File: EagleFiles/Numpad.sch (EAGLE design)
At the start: 67 parts, among them X1 52559-2492

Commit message: Readme added
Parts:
- removed COMM: SJ-43514_HEADPHONES_3.5MM_X4, my_parts:SJ-43514_HEADPHONES_3.5MM_X4
- removed R4, R5: 3.3K, resistor:R-US_0207/10
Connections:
- removed net N$51: COMM.4, R4.2, R5.1
- removed net N$52: COMM.3, R5.2
- removed net N$53: COMM.2, R4.1
- net GND: no longer COMM.1
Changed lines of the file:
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@@
 </classes>
 <parts>
-<part name="COMM" library="my_parts" deviceset="SJ-43514_HEADPHONES_3.5MM_X4" device=""/>
-<part name="SUPPLY3" library="supply2" deviceset="GND" device=""/>
-<part name="R4" library="resistor" deviceset="R-US_" device="0207/10" value="3.3K"/>
-<part name="R5" library="resistor" deviceset="R-US_" device="0207/10" value="3.3K"/>
 <part name="U$35" library="STM32F10x F4xx" deviceset="STM32F405/415_LQFP64" device=""/>
 <part name="C1" library="resistor" library_urn="urn:adsk.eagle:library:348" deviceset="C-US" device="C0603" package3d_urn="urn:adsk.eagle:package:23616/2" value="4.7uF"/>
@@
 </plain>
 <instances>
-<instance part="COMM" gate="G$1" x="-93.98" y="110.49" smashed="yes"/>
-<instance part="SUPPLY3" gate="GND" x="-80.01" y="97.79" smashed="yes">
-<attribute name="VALUE" x="-81.915" y="94.615" size="1.778" layer="96"/>
-</instance>
-<instance part="R4" gate="G$1" x="-54.61" y="123.19" smashed="yes" rot="R90">
-<attribute name="NAME" x="-56.1086" y="119.38" size="1.778" layer="95" rot="R90"/>
-<attribute name="VALUE" x="-51.308" y="119.38" size="1.778" layer="96" rot="R90"/>
-</instance>
-<instance part="R5" gate="G$1" x="-54.61" y="102.87" smashed="yes" rot="R90">
-<attribute name="NAME" x="-56.1086" y="99.06" size="1.778" layer="95" rot="R90"/>
-<attribute name="VALUE" x="-51.308" y="99.06" size="1.778" layer="96" rot="R90"/>
-</instance>
 <instance part="U$35" gate="G$1" x="86.24" y="83.92" smashed="yes" rot="R90"/>
 <instance part="C1" gate="G$1" x="119.26" y="35.66" smashed="yes">
@@
 <nets>
 <net name="GND" class="0">
-<segment>
-<pinref part="SUPPLY3" gate="GND" pin="GND"/>
-<pinref part="COMM" gate="G$1" pin="1"/>
-<wire x1="-80.01" y1="100.33" x2="-80.01" y2="102.87" width="0.1524" layer="91"/>
-<wire x1="-80.01" y1="102.87" x2="-81.28" y2="102.87" width="0.1524" layer="91"/>
-</segment>
 <segment>
 <pinref part="C_VCAP2" gate="G$1" pin="2"/>
@@
 </segment>
 </net>
-<net name="N$51" class="0">
-<segment>
-<wire x1="-60.96" y1="128.27" x2="-60.96" y2="134.62" width="0.1524" layer="91"/>
-<wire x1="-60.96" y1="134.62" x2="-60.96" y2="168.91" width="0.1524" layer="91"/>
-<pinref part="R4" gate="G$1" pin="2"/>
-<wire x1="-54.61" y1="128.27" x2="-60.96" y2="128.27" width="0.1524" layer="91"/>
-<wire x1="-60.96" y1="134.62" x2="-48.26" y2="134.62" width="0.1524" layer="91"/>
-<wire x1="-48.26" y1="134.62" x2="-48.26" y2="97.79" width="0.1524" layer="91"/>
-<junction x="-60.96" y="134.62"/>
-<pinref part="R5" gate="G$1" pin="1"/>
-<wire x1="-48.26" y1="97.79" x2="-54.61" y2="97.79" width="0.1524" layer="91"/>
-<pinref part="COMM" gate="G$1" pin="4"/>
-<wire x1="-81.28" y1="120.65" x2="-60.96" y2="120.65" width="0.1524" layer="91"/>
-<wire x1="-60.96" y1="120.65" x2="-60.96" y2="128.27" width="0.1524" layer="91"/>
-<junction x="-60.96" y="128.27"/>
-</segment>
-</net>
-<net name="N$52" class="0">
-<segment>
-<pinref part="COMM" gate="G$1" pin="3"/>
-<wire x1="-81.28" y1="107.95" x2="-54.61" y2="107.95" width="0.1524" layer="91"/>
-<pinref part="R5" gate="G$1" pin="2"/>
-</segment>
-</net>
-<net name="N$53" class="0">
-<segment>
-<pinref part="COMM" gate="G$1" pin="2"/>
-<wire x1="-81.28" y1="118.11" x2="-54.61" y2="118.11" width="0.1524" layer="91"/>
-<pinref part="R4" gate="G$1" pin="1"/>
-</segment>
-</net>

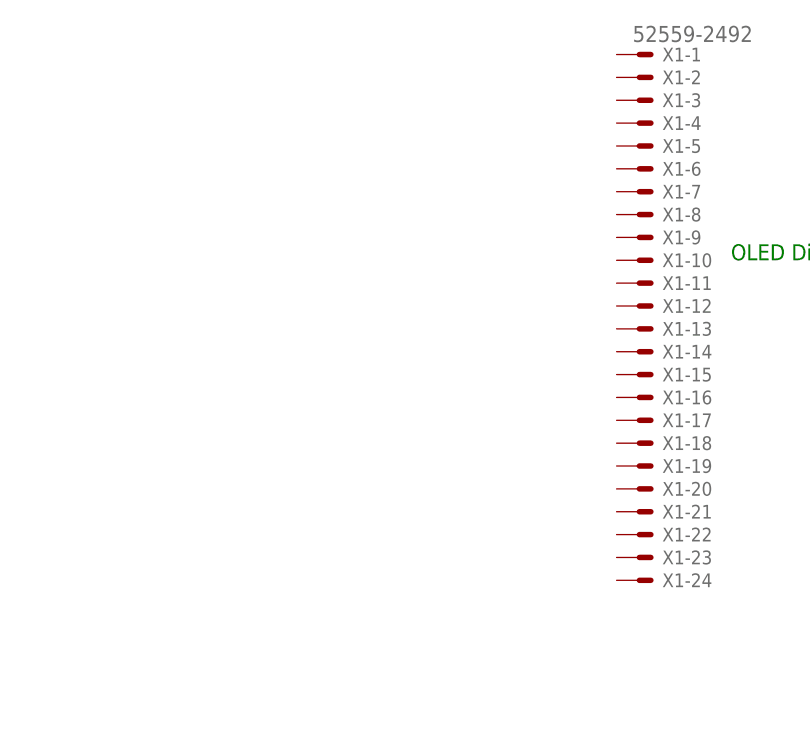
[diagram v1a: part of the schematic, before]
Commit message: Oled schematic added
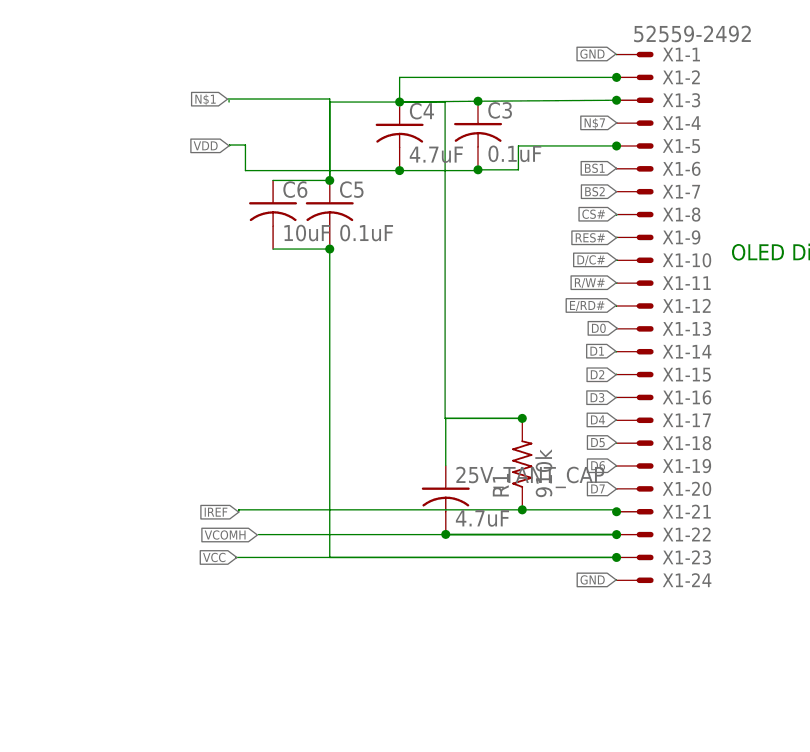
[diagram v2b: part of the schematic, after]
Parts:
- added 25V_TANT_CAP: 4.7uF, rcl:C-USC0805
- added C3, C5: 0.1uF, resistor:C-USC0603
- added C4: 4.7uF, resistor:C-USC0603
- added C6: 10uF, resistor:C-USC0603
- added R1: 910k, resistor:R-US_R0603
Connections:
- new net BS1: X1-6.S
- new net BS2: X1-7.S
- new net CS#: X1-8.S
- new net D/C#: X1-10.S
- new net D0: X1-13.S
- new net D1: X1-14.S
- new net D2: X1-15.S
- new net D3: X1-16.S
- new net D4: X1-17.S
- new net D5: X1-18.S
- new net D6: X1-19.S
- new net D7: X1-20.S
- new net E/RD#: X1-12.S
- new net IREF: R1.1, X1-21.S
- new net N$7: X1-4.S
- new net R/W#: X1-11.S
- new net RES#: X1-9.S
- new net VCC: C5.2, C6.2, X1-23.S
- new net VCOMH: 25V_TANT_CAP.2, X1-22.S
- new net VDD: C3.2, C4.2, X1-5.S
- new net VLSS: 25V_TANT_CAP.1, C3.1, C4.1, C5.1, C6.1, R1.2, X1-2.S, X1-3.S
- net GND: now also X1-1.S, X1-24.S
